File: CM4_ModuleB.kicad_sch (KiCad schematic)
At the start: 1 part

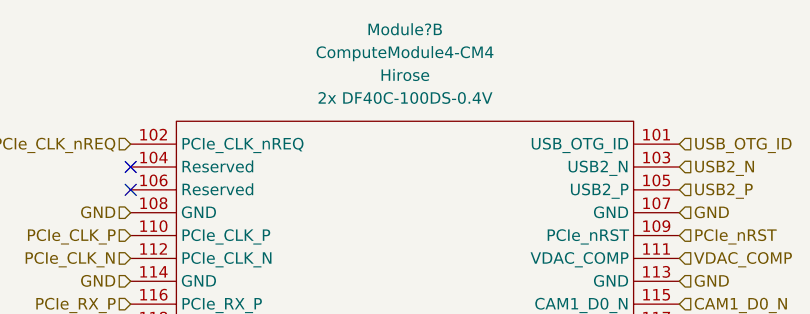
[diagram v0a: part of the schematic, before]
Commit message: PCB ready to trace
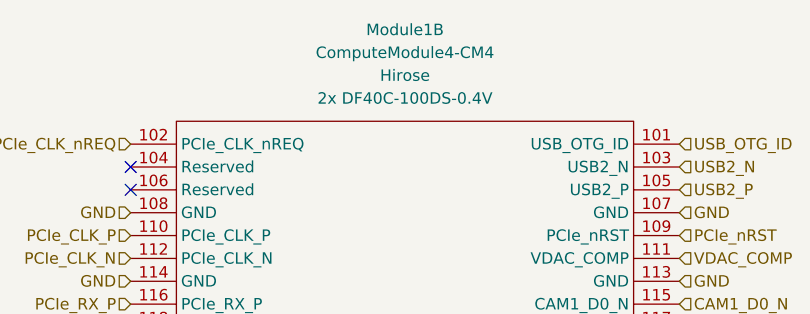
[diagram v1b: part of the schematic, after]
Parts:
- gave numbers to parts that had none: 1
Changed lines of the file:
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@@
   (symbol (lib_id "CM4IO:ComputeModule4-CM4") (at 8.89 93.98 0) (unit 2)
     (in_bom yes) (on_board yes)
-    (property "Reference" "Module?" (id 0) (at 148.59 20.32 0))
+    (property "Reference" "Module1" (id 0) (at 148.59 20.32 0))
     (property "Value" "ComputeModule4-CM4" (id 1) (at 148.59 22.86 0))
     (property "Footprint" "CM4IO:Raspberry-Pi-4-Compute-Module" (id 2) (at 151.13 120.65 0)
